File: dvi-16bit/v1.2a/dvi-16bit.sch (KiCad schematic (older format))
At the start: 30 parts, among them J1 PMOD, J10 Jumper_NO_Small, J2 PMOD, J4 Conn_02x03_Odd_Even, J5 3v3_5v_sel, J6 HDMI_A_1.4, J7 sj, J8 sj, J9 sj, U2 SII164

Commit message: more fixes
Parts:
- renumbered R5 to R2, R6 to R3, R7 to R4, R9 to R5
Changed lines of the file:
@@
 	7600 3200 7600 2300
 $Comp
-L Device:R_Small R9
+L Device:R_Small R5
 U 1 1 5B0DC406
 P 7600 2200
-F 0 "R9" H 7659 2247 50  0000 L CNN
+F 0 "R5" H 7659 2247 50  0000 L CNN
 F 1 "510E" H 7659 2154 50  0000 L CNN
 F 2 "Resistor_SMD:R_0603_1608Metric_Pad0.98x0.95mm_HandSolder" H 7659 2107 60  0001 L CNN
@@
 	5700 4600 5050 4600
 $Comp
-L Device:R_Small R6
+L Device:R_Small R3
 U 1 1 5B16B43B
 P 5050 6100
-F 0 "R6" V 5050 6050 50  0000 L CNN
+F 0 "R3" V 5050 6050 50  0000 L CNN
 F 1 "DNP" V 5100 6200 50  0000 L CNN
 F 2 "Resistor_SMD:R_0603_1608Metric_Pad0.98x0.95mm_HandSolder" H 5109 6007 60  0001 L CNN
@@
 $EndComp
 $Comp
-L Device:R_Small R7
+L Device:R_Small R4
 U 1 1 5B395815
 P 5150 6100
-F 0 "R7" V 5150 6050 50  0000 L CNN
+F 0 "R4" V 5150 6050 50  0000 L CNN
 F 1 "10k" V 5200 6200 50  0000 L CNN
 F 2 "Resistor_SMD:R_0603_1608Metric_Pad0.98x0.95mm_HandSolder" H 5209 6007 60  0001 L CNN
@@
 	5150 6200 5150 6300
 $Comp
-L Device:R_Small R5
+L Device:R_Small R2
 U 1 1 5B14D068
 P 5050 4400
-F 0 "R5" V 5050 4350 50  0000 L CNN
+F 0 "R2" V 5050 4350 50  0000 L CNN
 F 1 "33k" V 5100 4500 50  0000 L CNN
 F 2 "Resistor_SMD:R_0603_1608Metric_Pad0.98x0.95mm_HandSolder" H 5109 4307 60  0001 L CNN

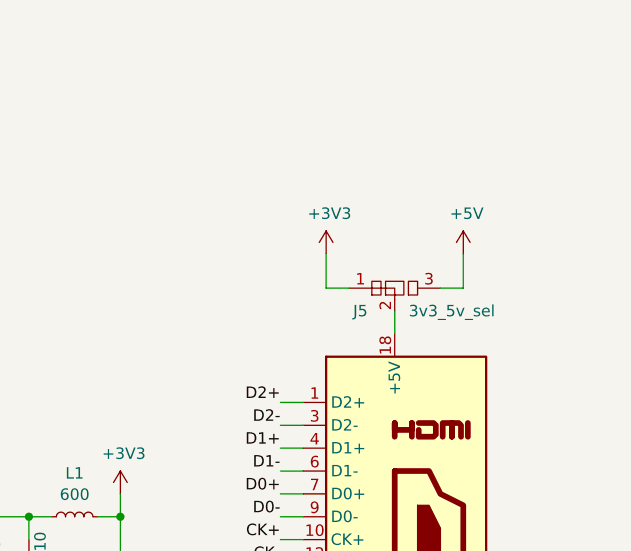
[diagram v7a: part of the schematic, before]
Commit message: fixed 5V/3V3 solderjumper for HDMI pin 18, and some other small fixes
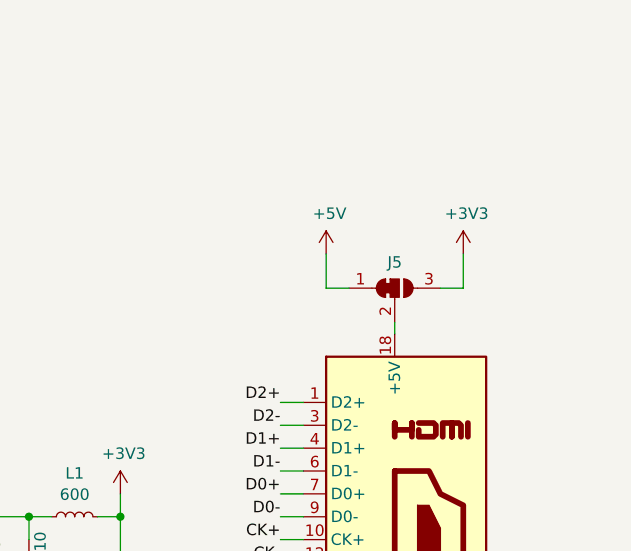
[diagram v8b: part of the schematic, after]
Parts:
- removed J5: 3v3_5v_sel, pkl_jumpers:J_NCNO_0903_30, symbol dvi-16bit-rescue:pkl_double_jumper_ncno-pkl_misc-dvi-12bit-rescue
- added J5: SolderJumper_3_Bridged12, Jumper:SolderJumper-3_P1.3mm_Bridged12_RoundedPad1.0x1.5mm, symbol Jumper:SolderJumper_3_Bridged12
- L1: footprint L_0603_1608Metric_Pad1.05x0.95mm_HandSolder -> Inductor_SMD:L_0603_1608Metric_Pad1.05x0.95mm_HandSolder
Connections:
- net +3V3: now also J5.3 (B)
- net +5V: now also J5.1 (A)
- net at J6.18 (+5V): now also J5.2 (C)
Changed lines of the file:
@@
 Text Notes 4950 5850 3    50   ~ 0
 91k for low-swing\ninput signal levels
-$Comp
-L Device:L_Small L1
-U 1 1 5B1838A6
-P 8700 3400
-F 0 "L1" V 8890 3400 50  0000 C CNN
-F 1 "600" V 8797 3400 50  0000 C CNN
-F 2 "L_0603_1608Metric_Pad1.05x0.95mm_HandSolder" H 8749 3307 60  0001 L CNN
-F 3 "" V 8700 3400 60  0001 C CNN
-F 4 "" H 8700 3400 50  0001 C CNN "Key"
-F 5 "" H 8700 3400 50  0001 C CNN "Source"
-	1    8700 3400
-	0    -1   -1   0
-$EndComp
 Wire Wire Line
 	8600 3400 8500 3400
@@
 	1    0    0    -1
 $EndComp
-Wire Wire Line
-	10100 2500 10100 2600
 $Comp
 L power:+5V #PWR0120
 U 1 1 5B3C4F78
-P 10400 2250
-F 0 "#PWR0120" H 10400 2100 50  0001 C CNN
-F 1 "+5V" H 10415 2426 50  0000 C CNN
-F 2 "" H 10400 2250 50  0001 C CNN
-F 3 "" H 10400 2250 50  0001 C CNN
-	1    10400 2250
+P 9800 2250
+F 0 "#PWR0120" H 9800 2100 50  0001 C CNN
+F 1 "+5V" H 9815 2426 50  0000 C CNN
+F 2 "" H 9800 2250 50  0001 C CNN
+F 3 "" H 9800 2250 50  0001 C CNN
+	1    9800 2250
 	1    0    0    -1
 $EndComp
@@
 Text Label 5600 3600 2    50   ~ 0
 B2
-$Comp
-L dvi-16bit-rescue:pkl_double_jumper_ncno-pkl_misc-dvi-12bit-rescue J5
-U 1 1 5C5DF288
-P 10100 2400
-F 0 "J5" H 9950 2500 50  0000 C CNN
-F 1 "3v3_5v_sel" H 10350 2500 50  0000 C CNN
-F 2 "pkl_jumpers:J_NCNO_0903_30" H 10050 2400 50  0001 C CNN
-F 3 "" H 10050 2400 50  0001 C CNN
-	1    10100 2400
-	1    0    0    1
-$EndComp
 Wire Wire Line
 	10300 2400 10400 2400
@@
 L power:+3V3 #PWR0128
 U 1 1 5C5F0282
-P 9800 2250
-F 0 "#PWR0128" H 9800 2100 50  0001 C CNN
-F 1 "+3V3" H 9815 2426 50  0000 C CNN
-F 2 "" H 9800 2250 50  0001 C CNN
-F 3 "" H 9800 2250 50  0001 C CNN
-	1    9800 2250
+P 10400 2250
+F 0 "#PWR0128" H 10400 2100 50  0001 C CNN
+F 1 "+3V3" H 10415 2426 50  0000 C CNN
+F 2 "" H 10400 2250 50  0001 C CNN
+F 3 "" H 10400 2250 50  0001 C CNN
+	1    10400 2250
 	1    0    0    -1
 $EndComp
@@
 	4600 4650 4600 4700
 $Comp
-L power:GND #PWR?
+L power:GND #PWR0107
 U 1 1 64FA2621
 P 4900 4250
-F 0 "#PWR?" H 4900 4000 50  0001 C CNN
+F 0 "#PWR0107" H 4900 4000 50  0001 C CNN
 F 1 "GND" H 4900 4100 50  0000 C CNN
 F 2 "" H 4900 4250 50  0001 C CNN
@@
 Wire Wire Line
 	4900 5800 5700 5800
+$Comp
+L Jumper:SolderJumper_3_Bridged12 J5
+U 1 1 6510DFD2
+P 10100 2400
+F 0 "J5" H 10100 2513 50  0000 C CNN
+F 1 "SolderJumper_3_Bridged12" H 10100 2514 50  0001 C CNN
+F 2 "Jumper:SolderJumper-3_P1.3mm_Bridged12_RoundedPad1.0x1.5mm" H 10100 2400 50  0001 C CNN
+F 3 "~" H 10100 2400 50  0001 C CNN
+	1    10100 2400
+	1    0    0    -1
+$EndComp
+Wire Wire Line
+	10100 2550 10100 2600
+$Comp
+L Device:L_Small L1
+U 1 1 64B6C5CA
+P 8700 3400
+F 0 "L1" V 8890 3400 50  0000 C CNN
+F 1 "600" V 8797 3400 50  0000 C CNN
+F 2 "Inductor_SMD:L_0603_1608Metric_Pad1.05x0.95mm_HandSolder" H 8749 3307 60  0001 L CNN
+F 3 "" V 8700 3400 60  0001 C CNN
+F 4 "" H 8700 3400 50  0001 C CNN "Key"
+F 5 "" H 8700 3400 50  0001 C CNN "Source"
+	1    8700 3400
+	0    -1   -1   0
+$EndComp
 $EndSCHEMATC
